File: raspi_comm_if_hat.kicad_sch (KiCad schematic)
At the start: 20 parts, among them J1 Conn_01x04, J2 Conn_01x04, J3 Conn_01x04, J4 Conn_02x20_Odd_Even, Q1 Q_PMOS_GSD, Q2 Q_PMOS_GSD, SW1 SW_SPDT, SW2 SW_DIP_x01, U1 MCP25625-x-SS, Y1 Resonator_Small

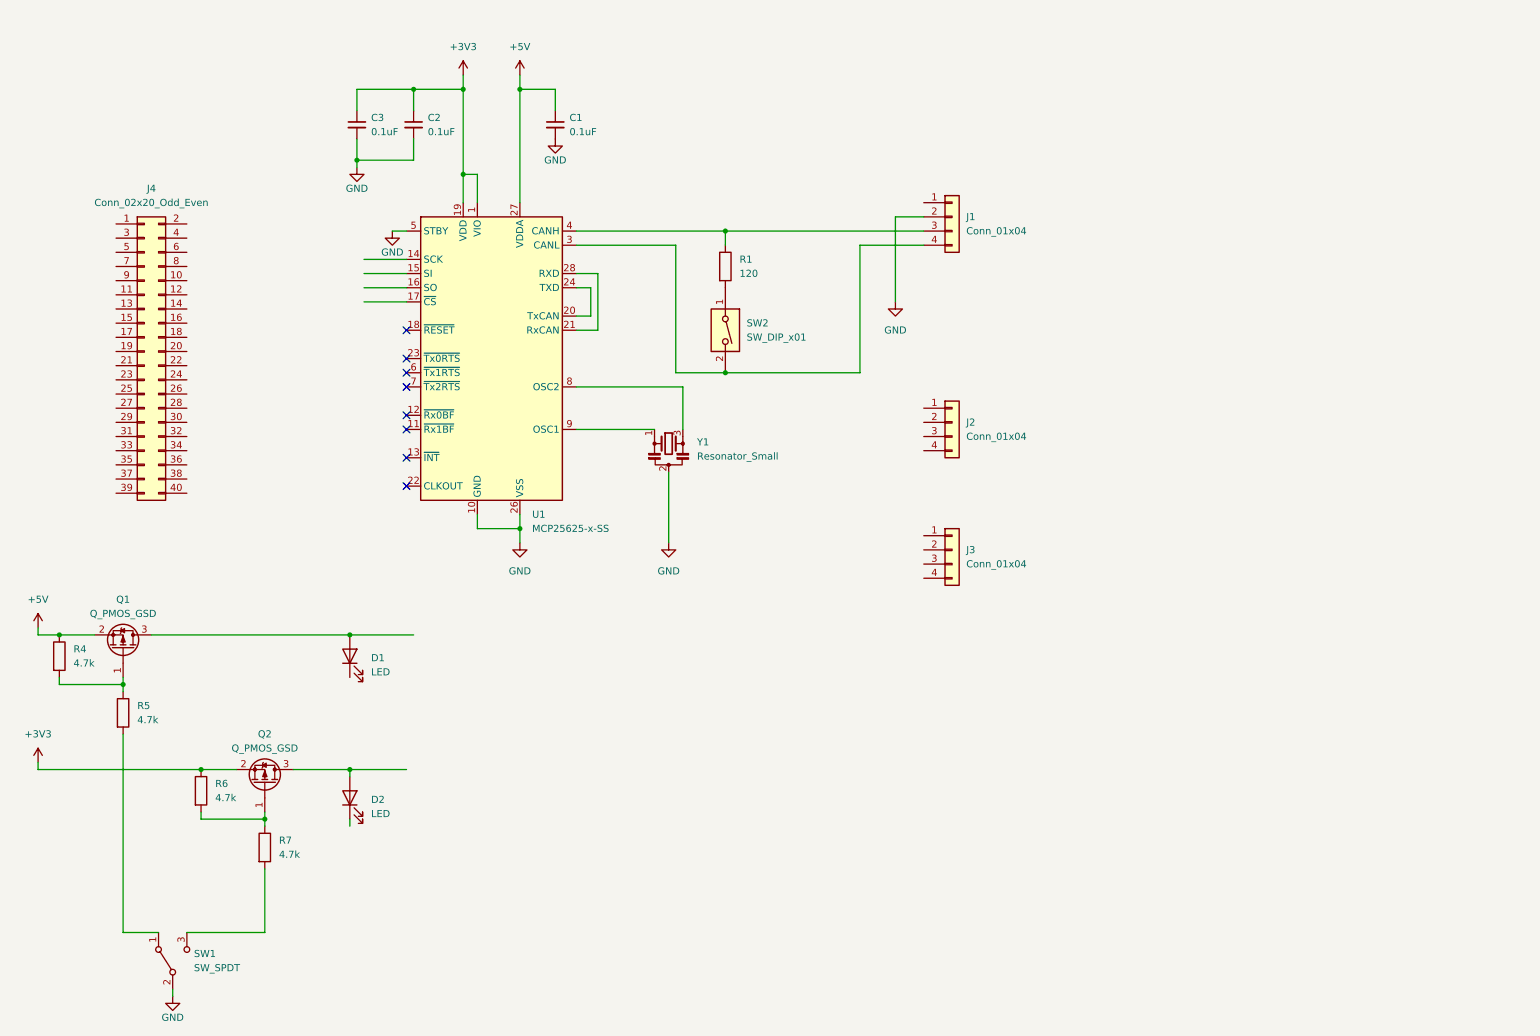
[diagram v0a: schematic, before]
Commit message: draw schemtic & PCB
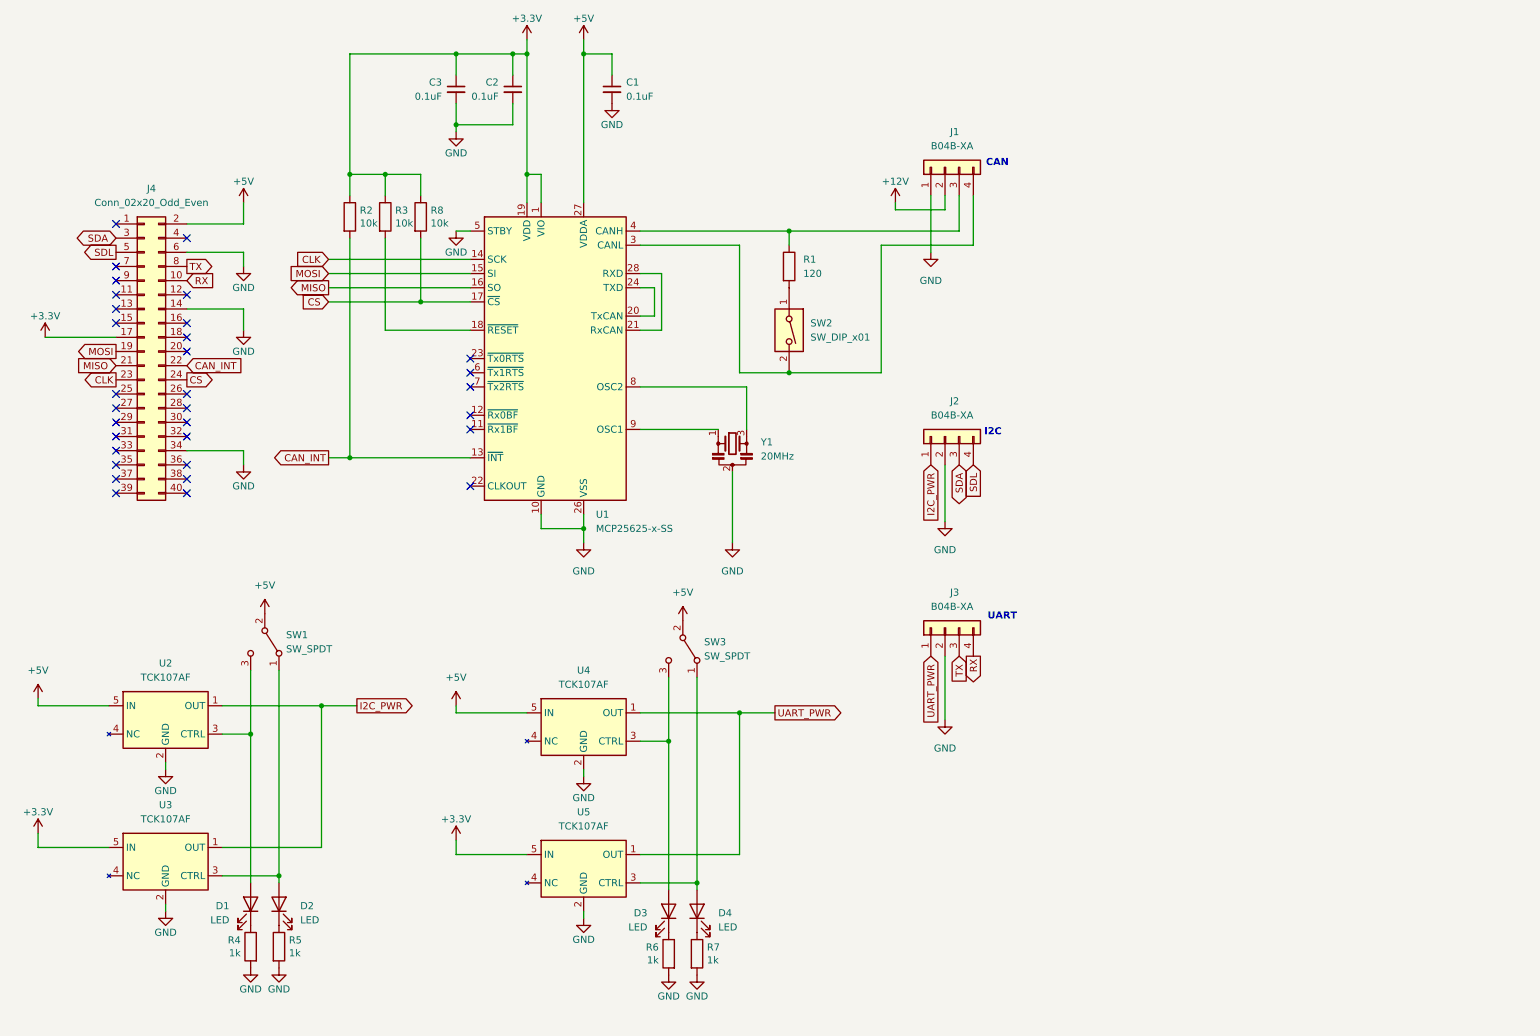
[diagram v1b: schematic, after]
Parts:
- removed Q1, Q2: Q_PMOS_GSD, Package_TO_SOT_SMD:SOT-23, symbol Device:Q_PMOS_GSD
- added D3, D4: LED, LED_SMD:LED_0603_1608Metric, symbol Device:LED
- added R2, R3, R8: 10k, Resistor_SMD:R_0603_1608Metric_Pad0.98x0.95mm_HandSolder, symbol Device:R
- added SW3: SW_SPDT, symbol Switch:SW_SPDT
- added U2, U3, U4, U5: TCK107AF, Package_TO_SOT_SMD:SOT-23-5, symbol RDC_generic:TCK107AF
- J1, J2, J3: value Conn_01x04 -> B04B-XA
- R4, R5, R6, R7: value 4.7k -> 1k; footprint Resistor_SMD:R_0603_1608Metric -> Resistor_SMD:R_0603_1608Metric_Pad0.98x0.95mm_HandSolder
- SW2: footprint (none) -> Button_Switch_THT:SW_DIP_SPSTx01_Slide_6.7x4.1mm_W7.62mm_P2.54mm_LowProfile
- Y1: value Resonator_Small -> 20MHz
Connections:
- net +5V: now also J4.2 (Pin_2), SW1.2 (B), SW3.2 (B), U2.5 (IN), U4.5 (IN); no longer R4.1
- net GND: now also J1.1 (Pin_1), J2.2 (Pin_2), J3.2 (Pin_2), J4.14 (Pin_14), J4.34 (Pin_34), J4.6 (Pin_6), R4.2, R5.2, R6.2, R7.2, U2.2 (GND), U3.2 (GND), U4.2 (GND), U5.2 (GND); no longer J1.2 (Pin_2), SW1.2 (B)
- net RX: now reaches J4.10 (Pin_10)
- net RX: now also J3.4 (Pin_4)
- net +3.3V: now reaches J4.17 (Pin_17)
- net +3.3V: now also C2.1, C3.1, U1.1 (VIO), U1.19 (VDD), R2.1, R3.1, R8.1, U3.5 (IN), U5.5 (IN)
- net MOSI: now reaches J4.19 (Pin_19)
- net MOSI: now also U1.15 (SI)
- net MISO: now reaches J4.21 (Pin_21)
- net MISO: now also U1.16 (SO)
- net CAN_INT: now reaches J4.22 (Pin_22)
- net CAN_INT: now also U1.13 (~{INT}), R2.2
- net CLK: now reaches J4.23 (Pin_23)
- net CLK: now also U1.14 (SCK)
- net CS: now reaches J4.24 (Pin_24)
- net CS: now also U1.17 (~{CS}), R8.2
- net SDA: now reaches J4.3 (Pin_3)
- net SDA: now also J2.3 (Pin_3)
- net SDL: now reaches J4.5 (Pin_5)
- net SDL: now also J2.4 (Pin_4)
- net TX: now reaches J4.8 (Pin_8)
- net TX: now also J3.3 (Pin_3)
- net UART_PWR: now reaches J3.1 (Pin_1)
- net UART_PWR: now also U4.1 (OUT), U5.1 (OUT)
- net I2C_PWR: now reaches J2.1 (Pin_1)
- net I2C_PWR: now also U2.1 (OUT), U3.1 (OUT)
- net at D2.1 (K): now also R5.1
- net at D2.2 (A): now also SW1.1 (A), U3.3 (CTRL)
- net at SW1.3 (C): now also D1.2 (A), U2.3 (CTRL); no longer R7.2
- net at D1.1 (K): now also R4.1
- net at R7.1: now also D4.1 (K); no longer R6.2
- net at U1.18 (~{RESET}): now also R3.2
- removed net +3V3: C2.1, C3.1, R6.1, U1.1 (VIO), U1.19 (VDD)
- new net: D4.2 (A), SW3.1 (A), U5.3 (CTRL)
- new net: D3.1 (K), R6.1
- new net: D3.2 (A), SW3.3 (C), U4.3 (CTRL)
- new net +12V: J1.2 (Pin_2)
- no-connect marks 8 -> 32
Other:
- note added: "CAN"
- note added: "I2C"
- note added: "UART"
- moved on the sheet: C1, C2, C3, J1, J2, J3, R1, SW1, SW2, U1, Y1

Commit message: update pcb
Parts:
- added H1, H2, H3, H4: MountingHole, MountingHole:MountingHole_2.7mm_M2.5, symbol Mechanical:MountingHole
- SW1, SW3: footprint (none) -> Button_Switch_THT:SW_CuK_OS102011MA1QN1_SPDT_Angled
- U2, U3, U4, U5: value TCK107AF -> TCK106AF; symbol RDC_generic:TCK107AF -> RDC_generic:TCK106AF
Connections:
- net +3.3V: now also J4.1 (Pin_1)
- net GND: now also J4.25 (Pin_25), J4.30 (Pin_30), J4.39 (Pin_39), J4.9 (Pin_9)
- no-connect marks 32 -> 27

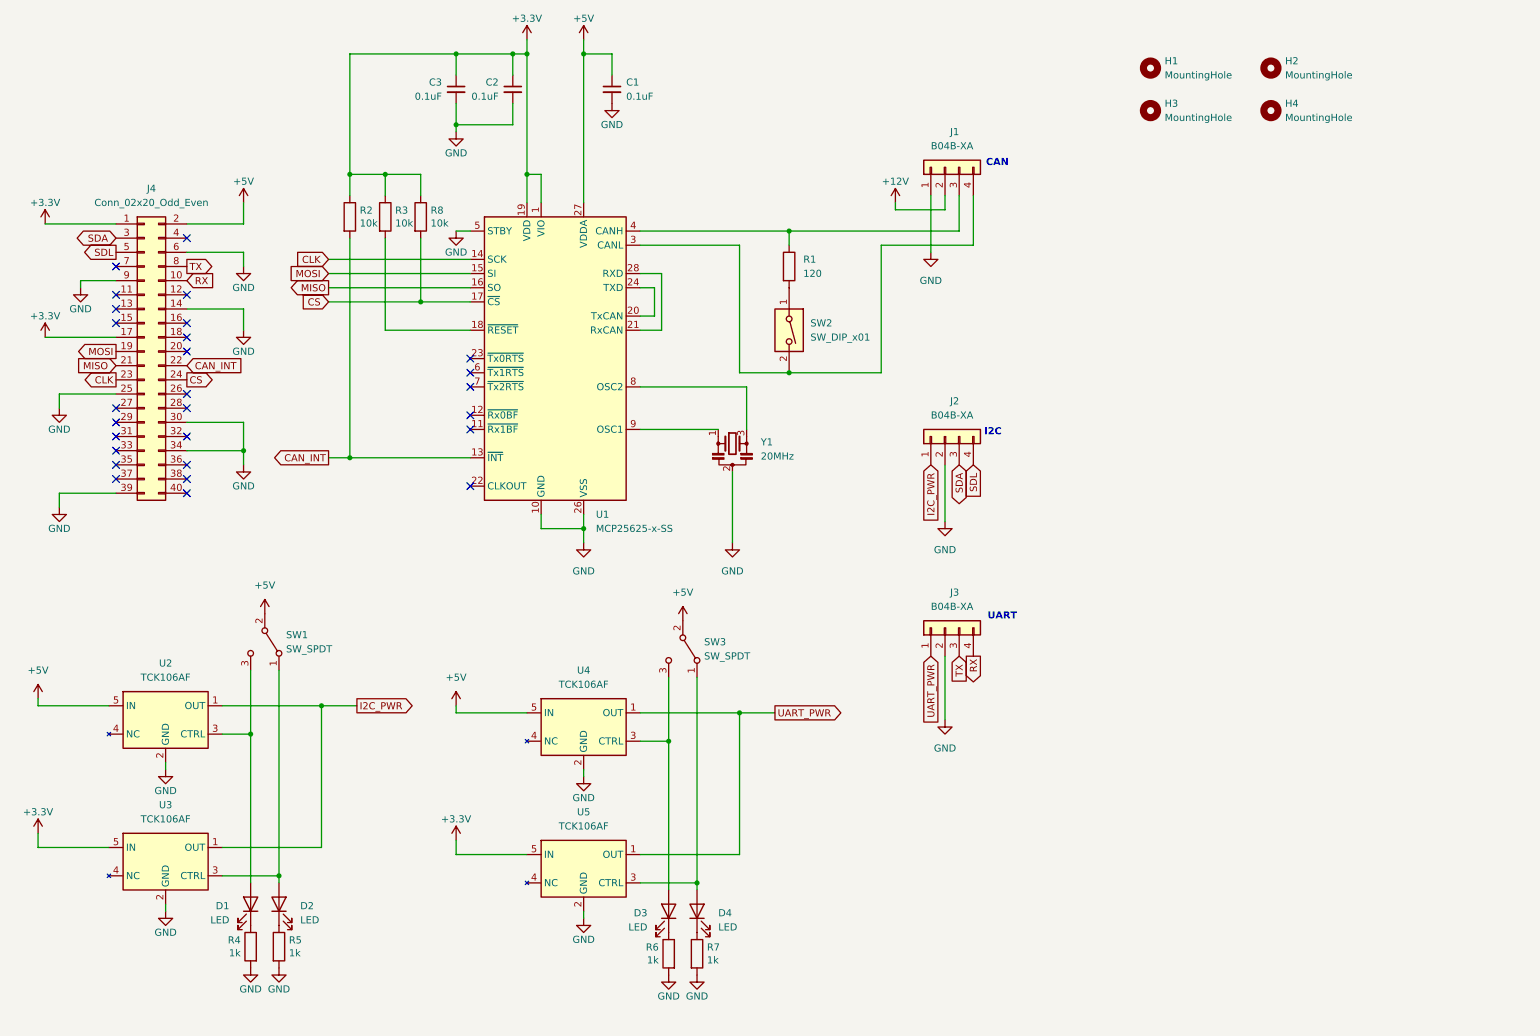
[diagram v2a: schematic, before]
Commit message: add fan connector
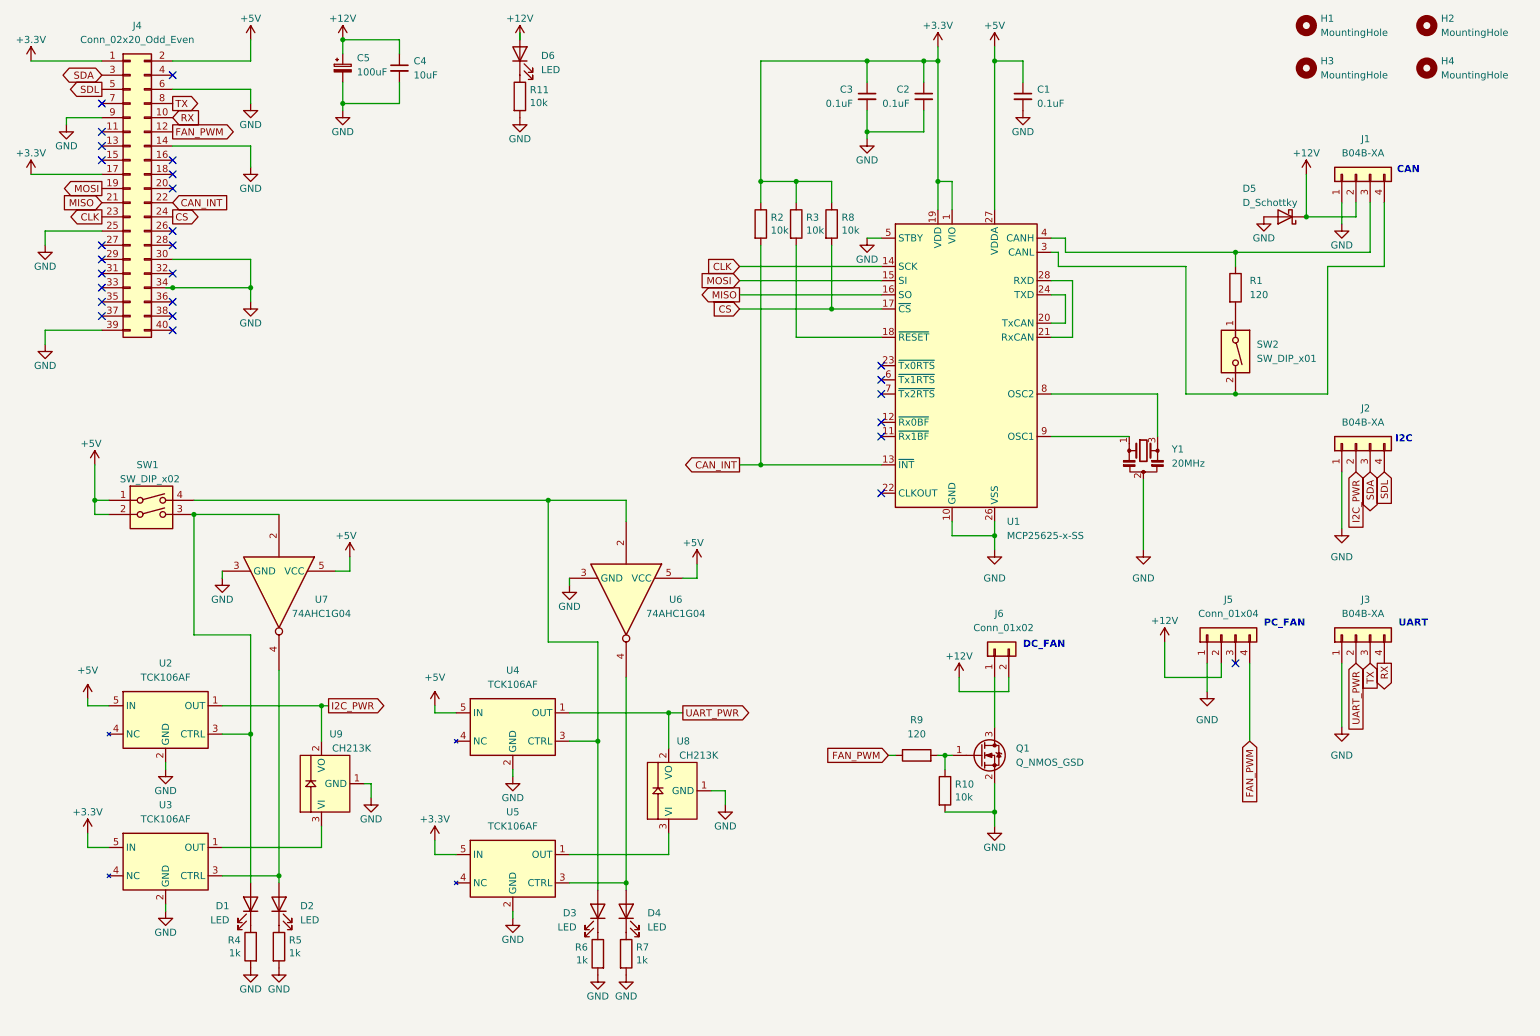
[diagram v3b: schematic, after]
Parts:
- removed SW1, SW3: SW_SPDT, Button_Switch_THT:SW_CuK_OS102011MA1QN1_SPDT_Angled, symbol Switch:SW_SPDT
- added C4: 10uF, symbol Device:C_Small
- added C5: 100uF, symbol Device:C_Polarized_Small
- added D5: D_Schottky, Diode_SMD:Vishay_SMPA, symbol Device:D_Schottky
- added D6: LED, LED_SMD:LED_0603_1608Metric, symbol Device:LED
- added J5: Conn_01x04, Connector_PinHeader_2.54mm:PinHeader_1x04_P2.54mm_Vertical, symbol Connector_Generic:Conn_01x04
- added J6: Conn_01x02, Connector_JST:JST_XA_B02B-XASK-1_1x02_P2.50mm_Vertical, symbol Connector_Generic:Conn_01x02
- added Q1: Q_NMOS_GSD, Package_TO_SOT_SMD:SOT-23, symbol Device:Q_NMOS_GSD
- added R10, R11: 10k, Resistor_SMD:R_0603_1608Metric_Pad0.98x0.95mm_HandSolder, symbol Device:R
- added R9: 120, Resistor_SMD:R_0603_1608Metric, symbol Device:R
- added SW1: SW_DIP_x02, Button_Switch_SMD:SW_DIP_SPSTx02_Slide_Copal_CHS-02B_W7.62mm_P1.27mm, symbol Switch:SW_DIP_x02
- added U6, U7: 74AHC1G04, Package_TO_SOT_SMD:SOT-23-5, symbol 74xGxx:74AHC1G04
- added U8, U9: CH213K, Package_TO_SOT_SMD:SOT-23, symbol RDC_generic:CH213K
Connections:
- net +12V: now also C4.1, C5.1, D5.1 (K), D6.2 (A), J5.2 (Pin_2), J6.2 (Pin_2)
- net +5V: now also SW1.1, SW1.2, U6.5 (VCC), U7.5 (VCC)
- net GND: now also J2.1 (Pin_1), J3.1 (Pin_1), C4.2, C5.2, D5.2 (A), J5.1 (Pin_1), Q1.2 (S), R10.2, R11.2, U6.3 (GND), U7.3 (GND), U8.1 (GND), U9.1 (GND); no longer J2.2 (Pin_2), J3.2 (Pin_2)
- net I2C_PWR: now also J2.2 (Pin_2), U9.2 (VO); no longer J2.1 (Pin_1), U3.1 (OUT)
- net UART_PWR: now also J3.2 (Pin_2), U8.2 (VO); no longer J3.1 (Pin_1), U5.1 (OUT)
- net FAN_PWM: now reaches J4.12 (Pin_12)
- net FAN_PWM: now also J5.4 (Pin_4), R9.1
- net at D4.2 (A), U5.3 (CTRL): now also U6.4
- net at D3.2 (A), U4.3 (CTRL): now also SW1.4, U6.2
- net at D2.2 (A), U3.3 (CTRL): now also U7.4
- net at D1.2 (A), U2.3 (CTRL): now also SW1.3, U7.2
- new net: Q1.1 (G), R10.1, R9.2
- new net: U5.1 (OUT), U8.3 (VI)
- new net: J6.1 (Pin_1), Q1.3 (D)
- new net: D6.1 (K), R11.1
- new net: U3.1 (OUT), U9.3 (VI)
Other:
- note added: "DC_FAN"
- note added: "PC_FAN"
- moved on the sheet: C1, C2, C3, D3, D4, H1, H2, H3, H4, J1, J2, J3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

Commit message: v0.1.0
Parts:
- removed C4: 10uF, symbol Device:C_Small
- added C1, C2: 10uF, Capacitor_SMD:C_0603_1608Metric, symbol Device:C_Small
- added C3, C8, C9: 0.1uF, Capacitor_SMD:C_0603_1608Metric, symbol Device:C_Small
- added R7, R8: 10k, Resistor_SMD:R_0603_1608Metric_Pad0.98x0.95mm_HandSolder, symbol Device:R
- C4: renamed from C5; footprint (none) -> Capacitor_Tantalum_SMD:CP_EIA-7343-15_Kemet-W
- renumbered C3 to C5, C2 to C6, C1 to C7, D6 to D1, D5 to D2, D1 to D3, D2 to D4, D3 to D5, D4 to D6, J4 to J2, J2 to J3, J6 to J4, J3 to J6, R11 to R1, R4 to R10, R5 to R11, R6 to R12, R7 to R13, R8 to R4, R1 to R5, R9 to R6, R10 to R9, SW2 to SW1, SW1 to SW2, U7 to U2, U6 to U3, U2 to U4, U4 to U5, U9 to U6, U8 to U7, U3 to U8, U5 to U9
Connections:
- net +3.3V: now also C2.1, C3.1
- net +5V: now also C1.1
- net GND: now also C1.2, C2.2, C3.2, C8.2, C9.2, R7.2, R8.2
- net I2C_PWR: now also C8.1, R7.1
- net RX: no longer J6.4 (Pin_4)
- net SDA: no longer J3.3 (Pin_3)
- net SDL: no longer J3.4 (Pin_4)
- net TX: no longer J6.3 (Pin_3)
- net UART_PWR: now also C9.1, R8.1
- new net RX_conn: J6.4 (Pin_4)
- new net SDA_conn: J3.3 (Pin_3)
- new net SDL_conn: J3.4 (Pin_4)
- new net TX_conn: J6.3 (Pin_3)
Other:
- added sheet Level_shifter (Level_shifter.kicad_sch)
- added sheet Level_shifter1 (Level_shifter.kicad_sch)
- moved on the sheet: C4, D1, D2, D5, D6, J1, J3, J4, J5, J6, Q1, R1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
